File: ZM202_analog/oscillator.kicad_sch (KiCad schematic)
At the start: 30 parts, among them U1 2N4416, U2 TL431, U3 LM324, U5 1N4148

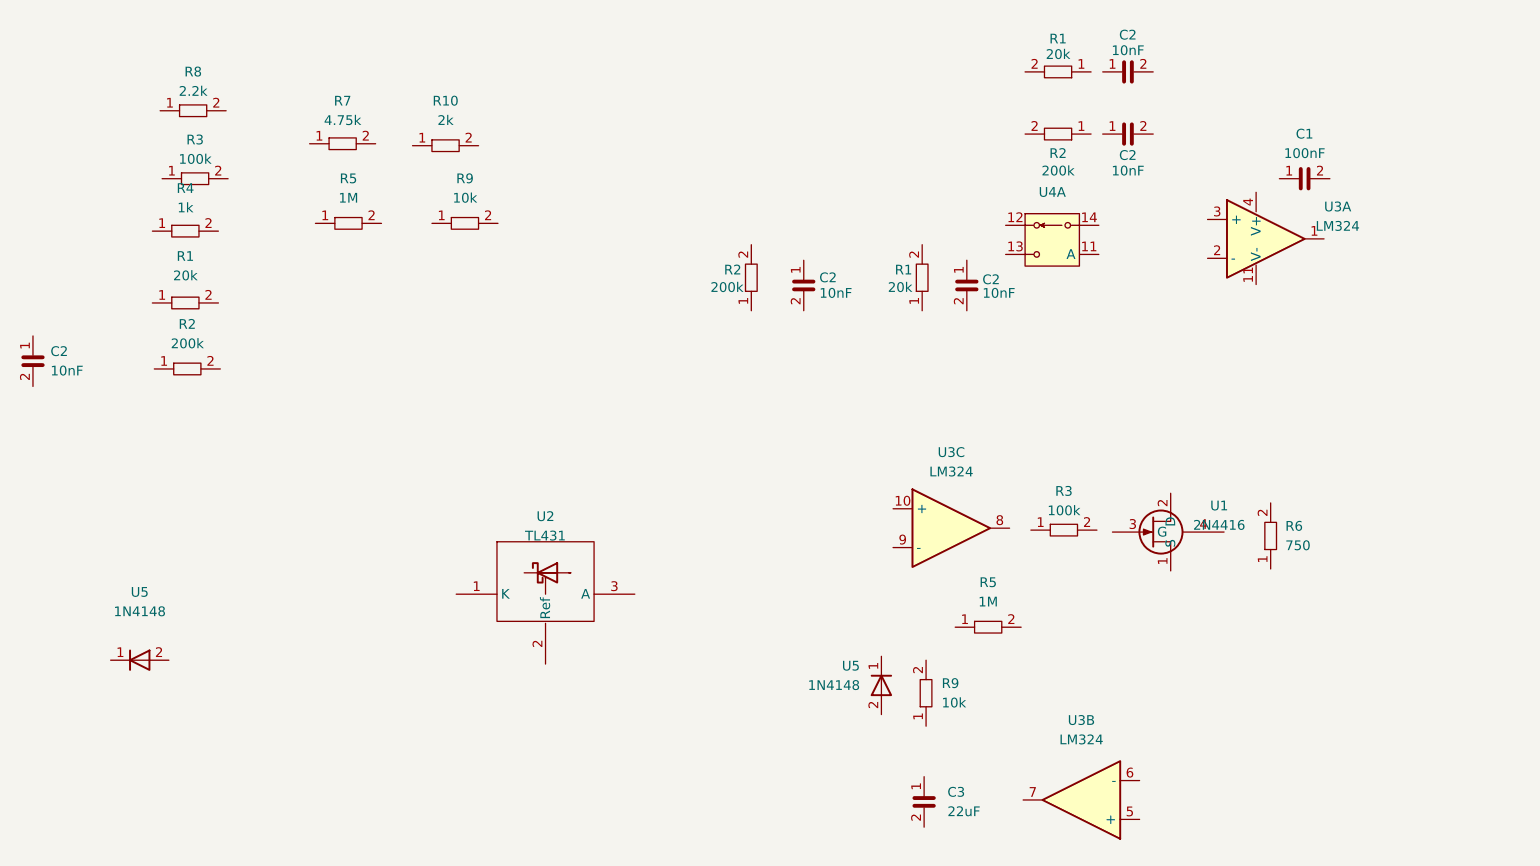
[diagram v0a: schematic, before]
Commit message: Oscillator is wired.
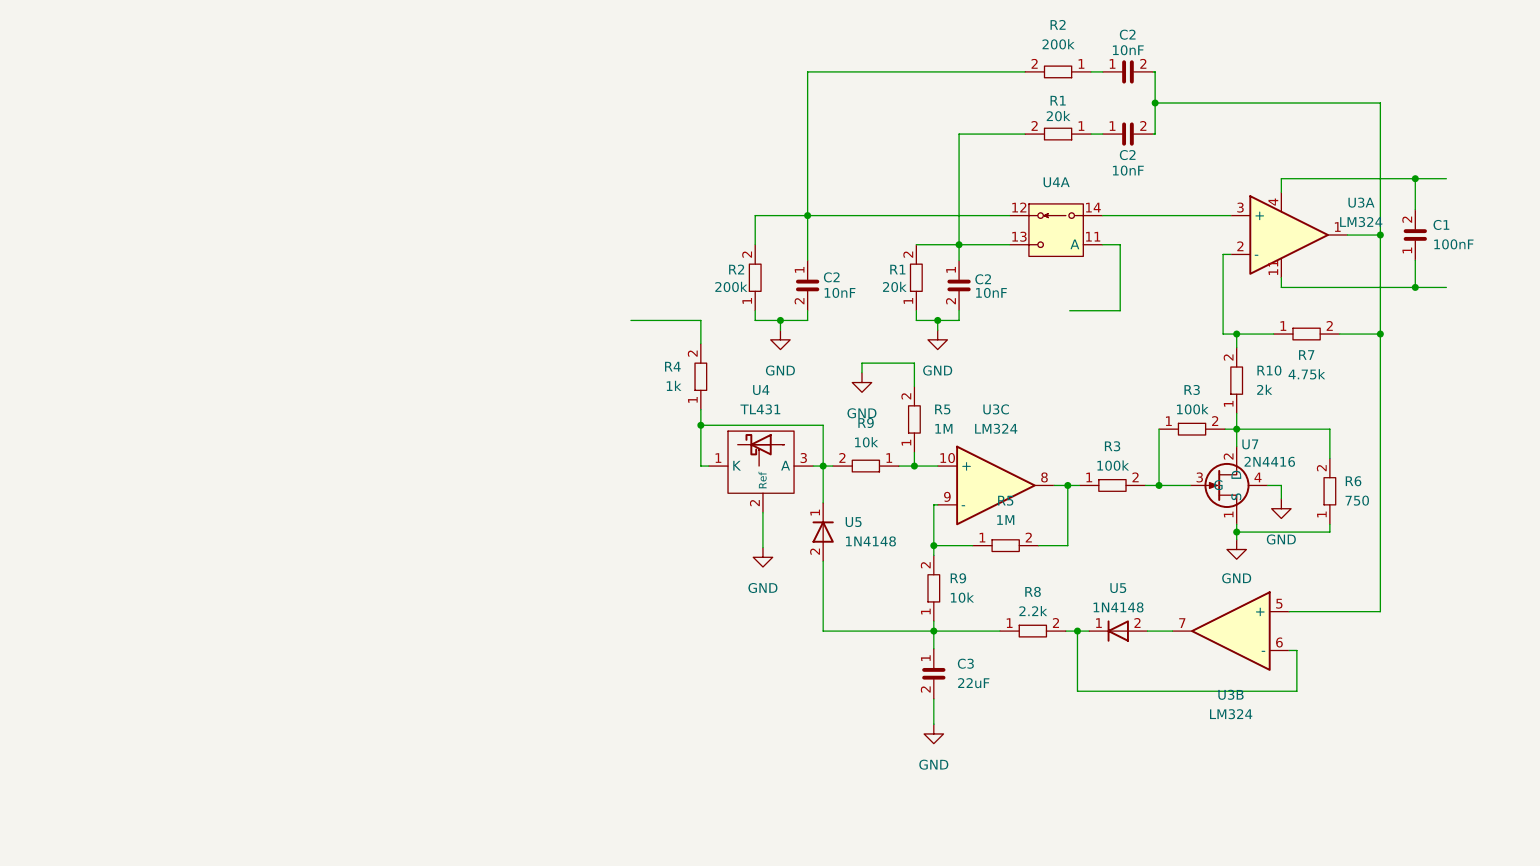
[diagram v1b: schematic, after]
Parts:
- removed C2: C0603_10nF_50V, Capacitor_SMD:C_0603_1608Metric, symbol Jojos_Lib:C0603_10nF_50V
- removed R1: R0603_20k, Resistor_SMD:R_0603_1608Metric, symbol Jojos_Lib:R0603_20k
- removed R2: R0603_200k, Resistor_SMD:R_0603_1608Metric, symbol Jojos_Lib:R0603_200k
- removed U1: 2N4416, Package_TO_SOT_THT:TO-72-4, symbol Jojo_Kicad_Lib:2N4416
- removed U2: TL431, Package_TO_SOT_SMD:SOT-23, symbol Jojo_Kicad_Lib:TL431
- added U4: TL431, Package_TO_SOT_SMD:SOT-23, symbol Jojos_Lib:TL431
- added U7: 2N4416, Package_TO_SOT_THT:TO-72-4, symbol Jojos_Lib:2N4416
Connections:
- net at R9.1: now also R5.1, U3.10 (+)
- net at R9.2: now also R4.1, U5.1, U4.1 (K), U4.3 (A)
- net at R8.1: now also C3.1, R9.1, U5.2
- net at R8.2: now also U3.6 (-), U5.1
- net at U4.12: now also C2.1, R2.2, R2.2
- net at U4.13: now also C2.1, R1.2, R1.2
- net at U4.14: now also U3.3 (+)
- net GND: now reaches C2.2
- net GND: now also C2.2, C3.2, R1.1, R2.1, R5.2, R6.1, U4.2 (Ref), U7.1 (S), U7.4
- net at R3.1: now also R3.2, U7.3 (G)
- net at R3.2: now also R10.1, R6.2, U7.2 (D)
- net at U5.2: now also U3.7
- net at C2.1: now also R1.1
- net at C2.2: now also C2.2, R7.2, U3.1, U3.5 (+)
- net at R7.1: now also R10.2, U3.2 (-)
- net at U3.11: now also C1.1
- net at U3.4: now also C1.2
- net at R2.1: now also C2.1
- net at R3.1: now also R5.2, U3.8
- net at R5.1: now also R9.2, U3.9 (-)
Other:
- moved on the sheet: C1, C2, C3, R1, R2, R3, R5, R6, R7, R9, U3B, U3C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

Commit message: Wired analog part.
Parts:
- removed C1: C0603_100nF_25V, Capacitor_SMD:C_0603_1608Metric, symbol Jojos_Lib:C0603_100nF_25V
- renumbered U4 to U5, U7 to U8

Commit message: Added labels and connections to outside-world.
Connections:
- net FREQ: now reaches U4.11 (A)
- net +5V: now reaches R4.2
- net OSC_out: now reaches C2.2, C2.2, R7.2, U3.1, U3.5 (+)
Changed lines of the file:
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@@
     (stroke (width 0) (type default))
   )
-  (wire (pts (xy 202.438 51.562) (xy 202.438 60.198))
+  (wire (pts (xy 202.438 51.562) (xy 202.438 53.594))
     (stroke (width 0) (type default))
   )
@@
     (stroke (width 0) (type default))
   )
+  (wire (pts (xy 236.474 50.292) (xy 243.84 50.292))
+    (stroke (width 0) (type default))
+  )
   (wire (pts (xy 162.306 80.518) (xy 163.576 80.518))
     (stroke (width 0) (type default))
@@
     (stroke (width 0) (type default))
   )
-  (wire (pts (xy 147.574 64.516) (xy 147.574 61.468))
+  (wire (pts (xy 147.574 64.516) (xy 147.574 63.754))
     (stroke (width 0) (type default))
   )
@@
     (stroke (width 0) (type default))
   )
-  (wire (pts (xy 138.43 61.468) (xy 147.574 61.468))
-    (stroke (width 0) (type default))
-  )
   (wire (pts (xy 178.054 102.108) (xy 186.69 102.108))
     (stroke (width 0) (type default))
@@
     (stroke (width 0) (type default))
   )
-  (wire (pts (xy 195.834 60.198) (xy 202.438 60.198))
-    (stroke (width 0) (type default))
+  (hierarchical_label "FREQ" (shape input) (at 202.438 53.594 270) (fields_autoplaced)
+    (effects (font (size 1.27 1.27)) (justify right))
+  )
+  (hierarchical_label "OSC_out" (shape input) (at 243.84 50.292 0) (fields_autoplaced)
+    (effects (font (size 1.27 1.27)) (justify left))
   )
   (symbol (lib_id "Jojos_Lib:TL431") (at 155.702 80.518 0) (unit 1)
@@
         )
       )
+    )
+  )
+  (symbol (lib_id "power:+5V") (at 147.574 63.754 0) (unit 1)
+    (in_bom yes) (on_board yes) (dnp no) (fields_autoplaced)
+    (property "Reference" "#PWR038" (at 147.574 67.564 0)
+      (effects (font (size 1.27 1.27)) hide)
+    )
+    (property "Value" "+5V" (at 147.574 59.436 0)
+      (effects (font (size 1.27 1.27)))
+    )
+    (property "Footprint" "" (at 147.574 63.754 0)
+      (effects (font (size 1.27 1.27)) hide)
+    )
+    (property "Datasheet" "" (at 147.574 63.754 0)
+      (effects (font (size 1.27 1.27)) hide)
+    )
+    (pin "1")
+    (instances
+      (project "ZM202_analog"
+        (path "/99a04650-e6a5-4da0-b985-3216476cb3cd/623fe2f9-a117-4b04-94d6-8c06947e3053"
+          (reference "#PWR038") (unit 1)
+        )
+      )

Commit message: Connected hierarchical outlets to connector.
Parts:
- added C1: C0603_100nF_25V, Capacitor_SMD:C_0603_1608Metric, symbol Jojos_Lib:C0603_100nF_25V
- added U1: LM324, Package_SO:SO-14_3.9x8.65mm_P1.27mm, symbol Jojos_Lib:LM324ADR
- added U2: ~, Package_SO:SOIC-16W_5.3x10.2mm_P1.27mm, symbol Jojos_Lib:CD4053
- renumbered U5 to U3, U8 to U6
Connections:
- net +5V: now also C1.2, U1.4 (+), U2.16 (VDD)
- net GND: now also U2.6 (INH), U2.8 (VSS)
- new net -5V: C1.1, U1.11 (-), U2.7 (VEE)

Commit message: Changed amplification resistor/cap in the analog core to 82nF/2.49k and did some various changes in the symbols and updated them into the schematic. Added PWR-flags
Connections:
- net OSC_out renamed OSC_OUT
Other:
- moved on the sheet: C1, U1E, U2D

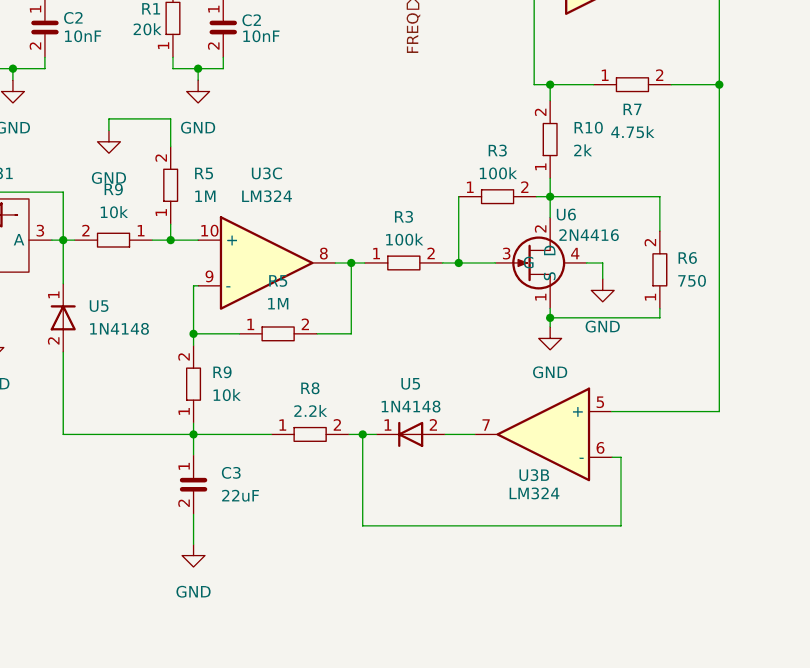
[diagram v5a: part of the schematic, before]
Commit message: Finished first version of PCB. Added some capacitors at digital ICs.
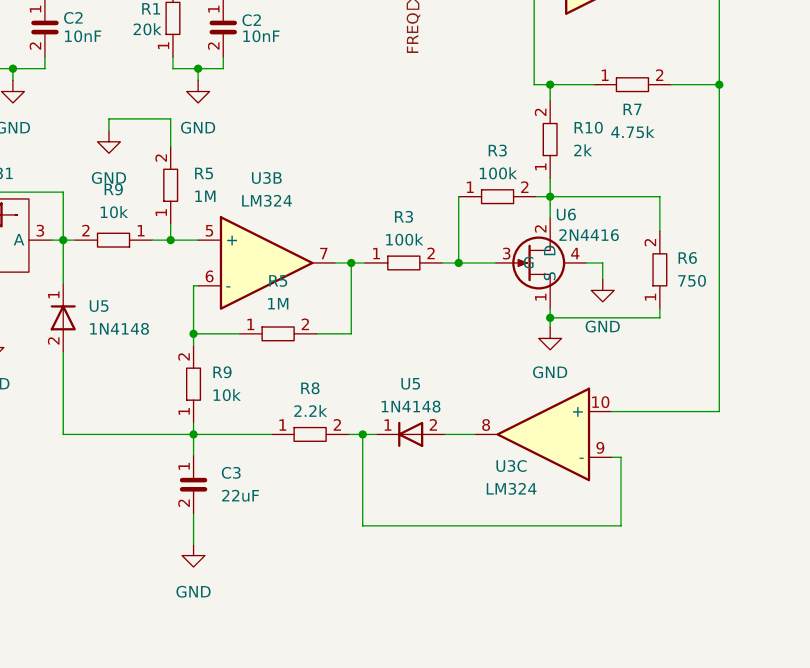
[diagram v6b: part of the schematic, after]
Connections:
- net OSC_OUT: now also U3.10 (+); no longer U3.5 (+)
- net at R5.1, R9.1: now also U3.5 (+); no longer U3.10 (+)
- net at R8.2, U5.1: now also U3.9 (-); no longer U3.6 (-)
- net at U5.2: now also U3.8; no longer U3.7
- net at R3.1, R5.2: now also U3.7; no longer U3.8
- net at R5.1, R9.2: now also U3.6 (-); no longer U3.9 (-)
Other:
- moved on the sheet: U3B, U3C
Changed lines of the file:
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@@
+    (stroke (width 0) (type default))
+  )
+  (wire (pts (xy 205.994 102.108) (xy 209.296 102.108))
     (stroke (width 0) (type default))
   )
@@
   )
   (wire (pts (xy 195.326 102.108) (xy 196.85 102.108))
-    (stroke (width 0) (type default))
-  )
-  (wire (pts (xy 205.994 102.108) (xy 209.296 102.108))
     (stroke (width 0) (type default))
   )
@@
     )
   )
-  (symbol (lib_id "Jojos_Lib:LM324ADR ") (at 219.456 102.108 0) (mirror y) (unit 2)
-    (in_bom yes) (on_board yes) (dnp no)
-    (property "Reference" "U3" (at 215.9 106.68 0)
-      (effects (font (size 1.27 1.27)))
-    )
-    (property "Value" "LM324" (at 215.9 108.712 0)
-      (effects (font (size 1.27 1.27)))
-    )
-    (property "Footprint" "Package_SO:SO-14_3.9x8.65mm_P1.27mm" (at 219.456 102.108 0)
-      (effects (font (size 1.27 1.27)) hide)
-    )
-    (property "Datasheet" "" (at 219.456 102.108 0)
-      (effects (font (size 1.27 1.27)) hide)
-    )
-    (property "Mouser Part Number" "595-LM324ADR " (at 219.456 102.108 0)
-      (effects (font (size 1.27 1.27)) hide)
-    )
-    (property "Place" "yes" (at 219.456 102.108 0)
+  (symbol (lib_id "Jojos_Lib:LM324ADR ") (at 183.642 83.058 0) (unit 2)
+    (in_bom yes) (on_board yes) (dnp no) (fields_autoplaced)
+    (property "Reference" "U3" (at 186.182 73.66 0)
+      (effects (font (size 1.27 1.27)))
+    )
+    (property "Value" "LM324" (at 186.182 76.2 0)
+      (effects (font (size 1.27 1.27)))
+    )
+    (property "Footprint" "Package_SO:SO-14_3.9x8.65mm_P1.27mm" (at 183.642 83.058 0)
+      (effects (font (size 1.27 1.27)) hide)
+    )
+    (property "Datasheet" "" (at 183.642 83.058 0)
+      (effects (font (size 1.27 1.27)) hide)
+    )
+    (property "Mouser Part Number" "595-LM324ADR " (at 183.642 83.058 0)
+      (effects (font (size 1.27 1.27)) hide)
+    )
+    (property "Place" "yes" (at 183.642 83.058 0)
       (effects (font (size 1.27 1.27)) hide)
     )
@@
     )
   )
-  (symbol (lib_id "Jojos_Lib:LM324ADR ") (at 183.642 83.058 0) (unit 3)
-    (in_bom yes) (on_board yes) (dnp no) (fields_autoplaced)
-    (property "Reference" "U3" (at 186.182 73.152 0)
-      (effects (font (size 1.27 1.27)))
-    )
-    (property "Value" "LM324" (at 186.182 75.692 0)
-      (effects (font (size 1.27 1.27)))
-    )
-    (property "Footprint" "Package_SO:SO-14_3.9x8.65mm_P1.27mm" (at 183.642 83.058 0)
-      (effects (font (size 1.27 1.27)) hide)
-    )
-    (property "Datasheet" "" (at 183.642 83.058 0)
-      (effects (font (size 1.27 1.27)) hide)
-    )
-    (property "Mouser Part Number" "595-LM324ADR " (at 183.642 83.058 0)
-      (effects (font (size 1.27 1.27)) hide)
-    )
-    (property "Place" "yes" (at 183.642 83.058 0)
-      (effects (font (size 1.27 1.27)) hide)
-    )
+  (symbol (lib_id "Jojos_Lib:LM324ADR ") (at 219.456 102.108 0) (mirror y) (unit 3)
+    (in_bom yes) (on_board yes) (dnp no)
+    (property "Reference" "U3" (at 213.36 105.664 0)
+      (effects (font (size 1.27 1.27)))
+    )
+    (property "Value" "LM324" (at 213.36 108.204 0)
+      (effects (font (size 1.27 1.27)))
+    )
+    (property "Footprint" "Package_SO:SO-14_3.9x8.65mm_P1.27mm" (at 219.456 102.108 0)
+      (effects (font (size 1.27 1.27)) hide)
+    )
+    (property "Datasheet" "" (at 219.456 102.108 0)
+      (effects (font (size 1.27 1.27)) hide)
+    )
+    (property "Mouser Part Number" "595-LM324ADR " (at 219.456 102.108 0)
+      (effects (font (size 1.27 1.27)) hide)
+    )
+    (property "Place" "yes" (at 219.456 102.108 0)
+      (effects (font (size 1.27 1.27)) hide)
+    )

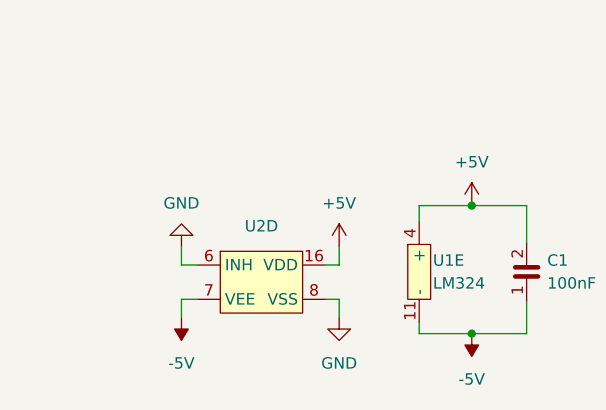
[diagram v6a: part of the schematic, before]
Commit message: New part placement.
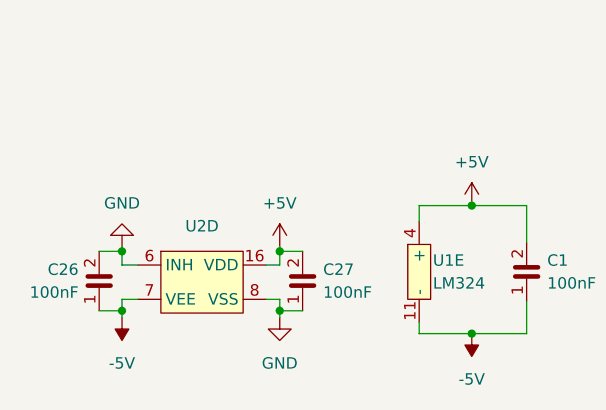
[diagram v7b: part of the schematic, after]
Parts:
- added C26, C27: C0603_100nF_25V, Capacitor_SMD:C_0603_1608Metric, symbol Jojos_Lib:C0603_100nF_25V
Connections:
- net +5V: now also C27.2
- net -5V: now also C26.1
- net GND: now also C26.2, C27.1
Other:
- moved on the sheet: U2D
